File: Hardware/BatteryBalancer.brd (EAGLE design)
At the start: 93.6 x 20.1 mm, 94 parts, among them IC1 OP-AMP, J2 ISP, U1 TAP_POINT, U10 MCP1755, U11 AD7280A, U12 ATMEGA328P_TQFP, U13 CH340C, U2 TAP_POINT, U3 TAP_POINT, U4 TAP_POINT, U5 TAP_POINT, Y1 16MHz

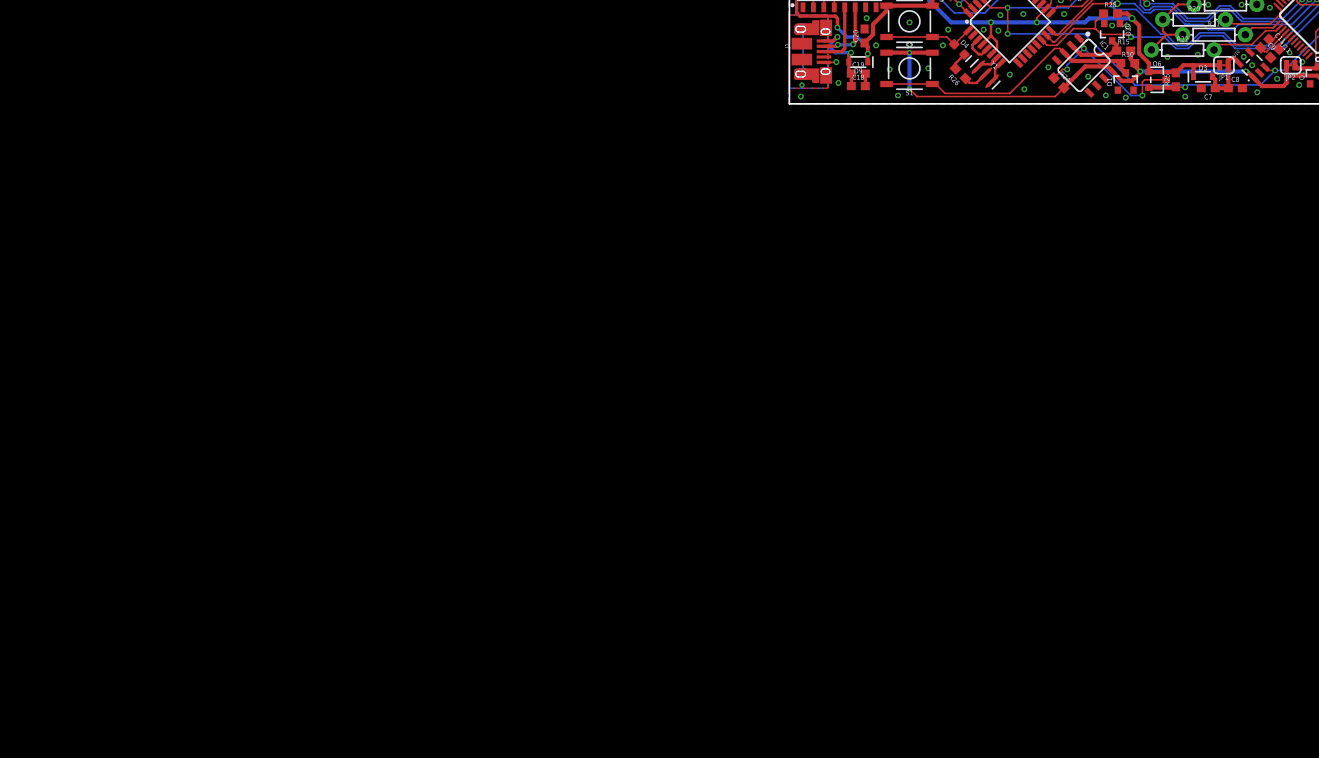
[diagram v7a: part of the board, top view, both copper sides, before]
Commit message: Implement LV shutoff circuit changes in schematic
Switch to voltage-divider/zener comparator, change regulator enable to raw compararator output
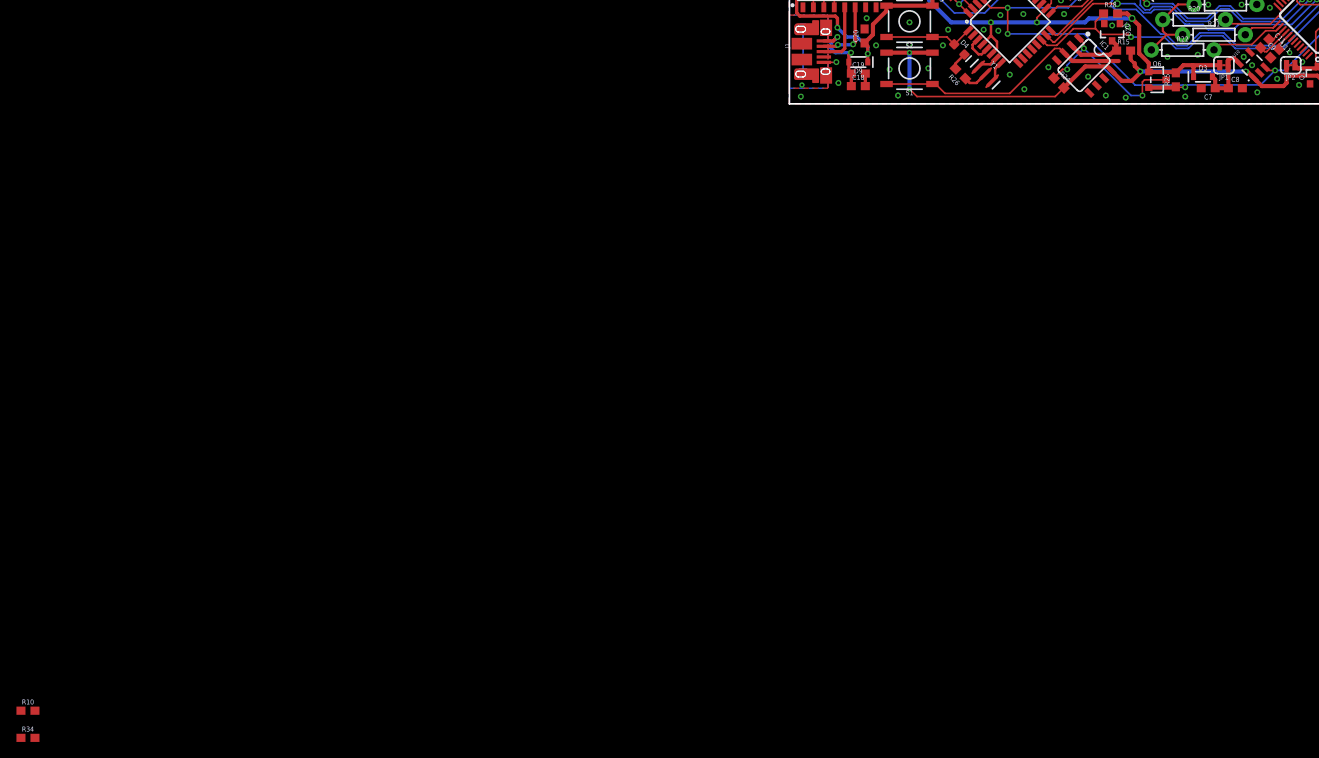
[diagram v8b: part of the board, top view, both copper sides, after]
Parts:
- removed D1: MATCH, SparkFun-DiscreteSemi:SOT23-3
- added R34: 10M, SparkFun-Resistors:0603
- D2: value TH -> TH-12V
- R10: value 1M -> 330k
- moved R10 155.2 mm to (-86.2, -43.8)
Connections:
- net CHARGE: now also U10.3
- net GND: now also R34.1; no longer D1.1
- net N$40: now also R34.2; no longer D1.3
- net RESET: no longer U10.3
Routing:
- net N$40: track 33.4 -> 31.6 mm
- net V_BATT: track 72.1 -> 71.3 mm
- net RESET: track 90.7 -> 90.1 mm
